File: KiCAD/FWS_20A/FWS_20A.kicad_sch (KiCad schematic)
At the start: 83 parts, among them J1 pwr, J2 Conn_01x02_Pin, J3 Conn_01x09_Socket, J4 Conn_01x02_Pin, J5 sense, Q1 DMN32D2LDF, Q6 DMN32D2LDF, SW2 SW_Push, U1 XMSM0L1306SRGER, U11 FCX495, U12 ADS1015IDGS, U2 FDMS8333L, U3 FDMS8333L, U4 LM5109BSD, U5 LM5109BSD, U6 L78L33_SO8, U7 FDMS8333L, U8 FDMS8333L

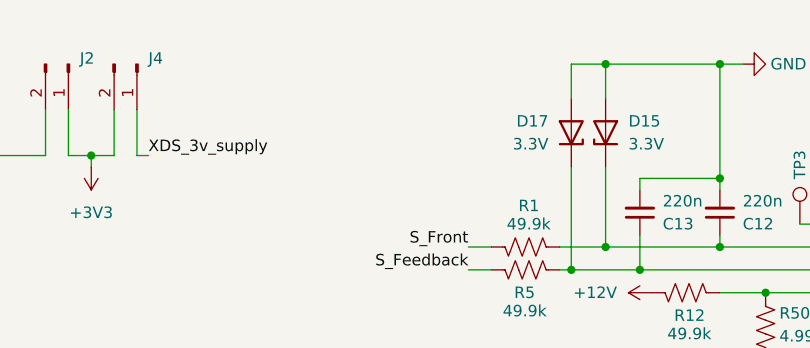
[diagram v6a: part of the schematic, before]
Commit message: more silkscreen txt
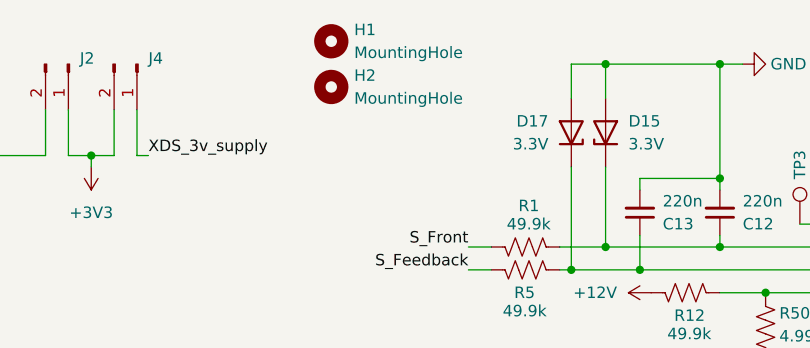
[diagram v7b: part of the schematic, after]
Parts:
- added H1, H2: MountingHole, MountingHole:MountingHole_2.2mm_M2_DIN965, symbol Mechanical:MountingHole
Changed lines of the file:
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@@
 	)
 	(symbol
+		(lib_id "Mechanical:MountingHole")
+		(at 173.99 21.59 0)
+		(unit 1)
+		(exclude_from_sim no)
+		(in_bom no)
+		(on_board yes)
+		(dnp no)
+		(fields_autoplaced yes)
+		(property "Reference" "H2"
+			(at 176.53 20.3199 0)
+			(effects
+				(font
+					(size 1.27 1.27)
+				)
+				(justify left)
+			)
+		)
+		(property "Value" "MountingHole"
+			(at 176.53 22.8599 0)
+			(effects
+				(font
+					(size 1.27 1.27)
+				)
+				(justify left)
+			)
+		)
+		(property "Footprint" "MountingHole:MountingHole_2.2mm_M2_DIN965"
+			(at 173.99 21.59 0)
+			(effects
+				(font
+					(size 1.27 1.27)
+				)
+				(hide yes)
+			)
+		)
+		(property "Datasheet" "~"
+			(at 173.99 21.59 0)
+			(effects
+				(font
+					(size 1.27 1.27)
+				)
+				(hide yes)
+			)
+		)
+		(property "Description" "Mounting Hole without connection"
+			(at 173.99 21.59 0)
+			(effects
+				(font
+					(size 1.27 1.27)
+				)
+				(hide yes)
+			)
+		)
+		(instances
+			(project "FWS_20A"
+				(path "/bd07da4b-c018-42fa-9039-1b3b7c5adf19"
+					(reference "H2")
+					(unit 1)
+				)
+			)
+		)
+	)
+	(symbol
 		(lib_id "Device:R_Small_US")
 		(at 81.28 157.48 270)
@@
 					(unit 1)
 				)
+			)
+		)
+	)
+	(symbol
+		(lib_id "Mechanical:MountingHole")
+		(at 173.99 16.51 0)
+		(unit 1)
+		(exclude_from_sim no)
+		(in_bom no)
+		(on_board yes)
+		(dnp no)
+		(fields_autoplaced yes)
+		(property "Reference" "H1"
+			(at 176.53 15.2399 0)
+			(effects
+				(font
+					(size 1.27 1.27)
+				)
+				(justify left)
+			)
+		)
+		(property "Value" "MountingHole"
+			(at 176.53 17.7799 0)
+			(effects
+				(font
+					(size 1.27 1.27)
+				)
+				(justify left)
+			)
+		)
+		(property "Footprint" "MountingHole:MountingHole_2.2mm_M2_DIN965"
+			(at 173.99 16.51 0)
+			(effects
+				(font
+					(size 1.27 1.27)
+				)
+				(hide yes)
+			)
+		)
+		(property "Datasheet" "~"
+			(at 173.99 16.51 0)
+			(effects
+				(font
+					(size 1.27 1.27)
+				)
+				(hide yes)
+			)
+		)
+		(property "Description" "Mounting Hole without connection"
+			(at 173.99 16.51 0)
+			(effects
+				(font
+					(size 1.27 1.27)
+				)
+				(hide yes)
+			)
+		)
+		(instances
+			(project ""
+				(path "/bd07da4b-c018-42fa-9039-1b3b7c5adf19"
+					(reference "H1")
+					(unit 1)
+				)

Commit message: cleaned up a bit
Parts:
- removed C12, C13: 220n, Capacitor_SMD:C_1206_3216Metric_Pad1.33x1.80mm_HandSolder, symbol Device:C_Small
- removed D15, D17: 3.3V, Diode_SMD:D_SOD-323, symbol Device:D_Zener
- removed J2, J4: Conn_01x02_Pin, Connector_PinHeader_2.54mm:PinHeader_1x02_P2.54mm_Vertical, symbol Connector:Conn_01x02_Pin
- removed R18, R23, R50: 4.99k, Resistor_SMD:R_1206_3216Metric_Pad1.30x1.75mm_HandSolder, symbol Device:R_US
- removed R5: 49.9k, Resistor_SMD:R_1206_3216Metric_Pad1.30x1.75mm_HandSolder, symbol Device:R_US
- removed TP3: TestPoint, TestPoint:TestPoint_Loop_D2.50mm_Drill1.0mm_LowProfile, symbol Connector:TestPoint
- removed TP4, TP5, TP6, TP7, TP8, TP9: TestPoint, TestPoint:TestPoint_Pad_D2.0mm, symbol Connector:TestPoint
- removed U12: ADS1015IDGS, Package_SO:TSSOP-10_3x3mm_P0.5mm, symbol Analog_ADC:ADS1015IDGS
- added C21: 220n, Capacitor_SMD:C_1206_3216Metric_Pad1.33x1.80mm_HandSolder, symbol Device:C_Small
- added D15, D17: BAT54S, Package_TO_SOT_SMD:SOT-23-3, symbol Diode:BAT54S
- added H3: MountingHole, MountingHole:MountingHole_2.2mm_M2_DIN965, symbol Mechanical:MountingHole
- added R22: 49.9k, Resistor_SMD:R_1206_3216Metric_Pad1.30x1.75mm_HandSolder, symbol Device:R_US
- added R5: 200k, Resistor_SMD:R_0805_2012Metric_Pad1.20x1.40mm_HandSolder, symbol Device:R_Small_US
- added U10, U9: MCP3421A0T-ECH, Package_TO_SOT_SMD:SOT-23-6, symbol Analog_ADC:MCP3421A0T-ECH
- added U18: L78L33_SO8, Package_SO:SOIC-8_3.9x4.9mm_P1.27mm, symbol Regulator_Linear:L78L33_SO8
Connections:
- net XDS_3v_supply is gone; now on net +3V3: J3.3 (Pin_3)
- net +12V: now also U18.8 (IN); no longer R12.2
- net +3V3: now also C11.1, U6.1 (OUT), D15.2 (K), D17.2 (K), U10.5 (V_{DD}), U9.5 (V_{DD})
- net GND: now also C21.2, D15.1 (A), D17.1 (A), U10.2 (V_{SS}), U10.6 (Vin-), U18.2 (GND), U18.3 (GND), U18.6 (GND), U18.7 (GND), U9.2 (V_{SS}), U9.6 (Vin-)
- net S_Feedback: now also R10.2
- net S_Front: now also R12.2; no longer R1.1
- net at R1.2: now also R10.1
- net at R12.1: now also R22.2
- net at C1.1, D1.1 (K), U11.1: now also R5.1; no longer R10.1
- net at D3.1 (K), U11.2: now also R5.2; no longer R10.2
- net Sensor Bias renamed Sensor_Supply
- net Sensor_Supply: now also C21.1, U18.1 (OUT)
- new net: D17.3 (COM), R22.1, U10.1 (Vin+)
- new net: D15.3 (COM), R1.1, U9.1 (Vin+)
- new net SCL: U10.3 (SCL), U9.3 (SCL)
- new net SDA: U10.4 (SDA), U9.4 (SDA)
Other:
- added sheet isolated TTL (isolated TTL.kicad_sch)
- note added: "improvements to be made - isolate the sensing components & power supplies. - protect against reverse polarity on sensor"
- moved on the sheet: C1, C14, C15, C2, C3, C4, C5, C6, C7, C8, C9, D1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
